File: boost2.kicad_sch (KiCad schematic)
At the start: 37 parts, among them Q1 BSC059N04LS6, Q2 BSC059N04LS6, U1 TPS43061

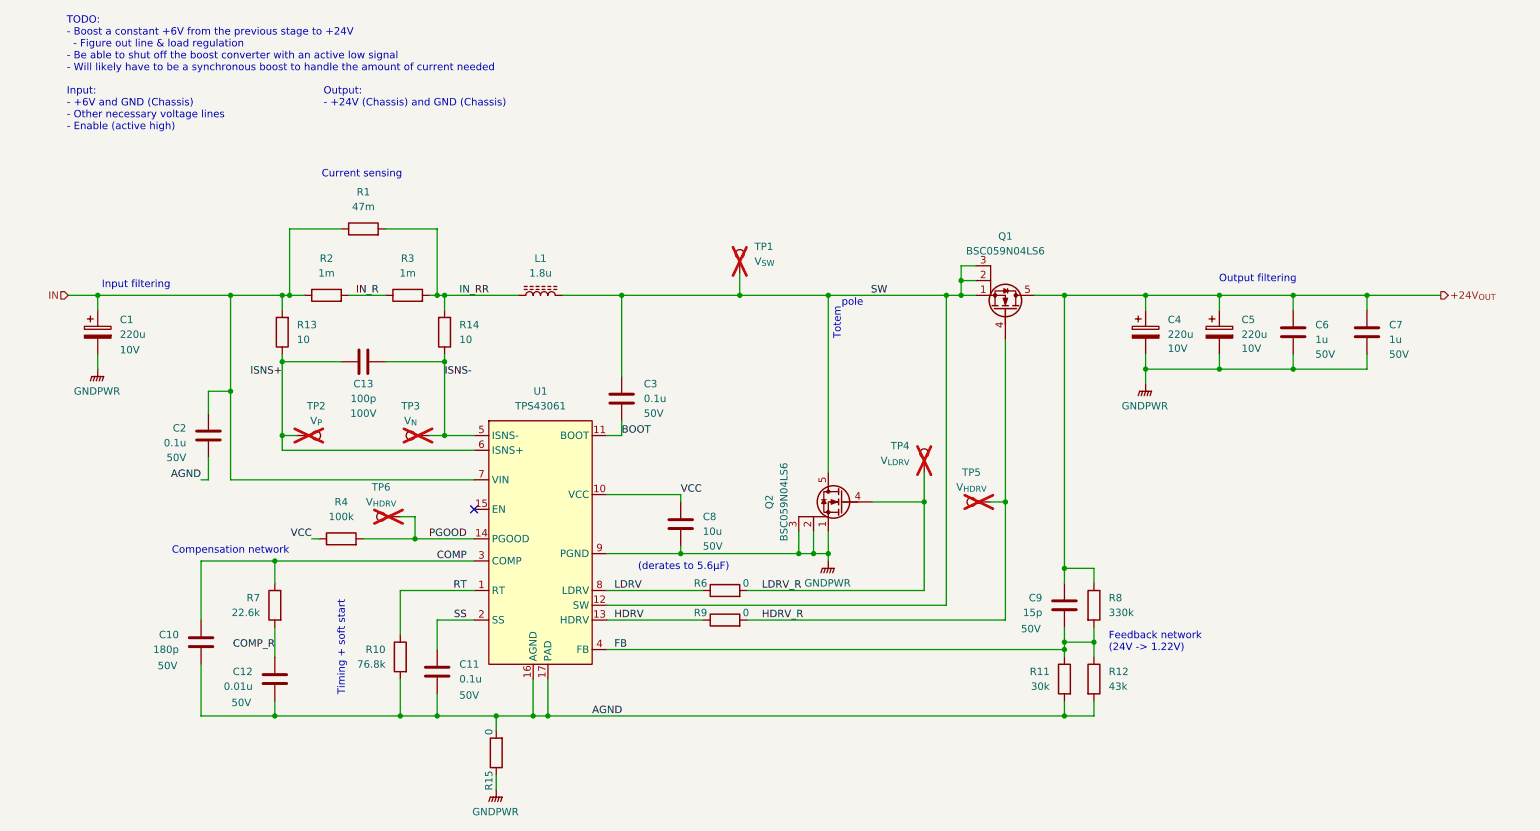
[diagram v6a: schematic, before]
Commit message: Adjust all PCBs and resize boards to be cheaper to order from JLCPCB
Also changed connector pinout to reflect silkscreen
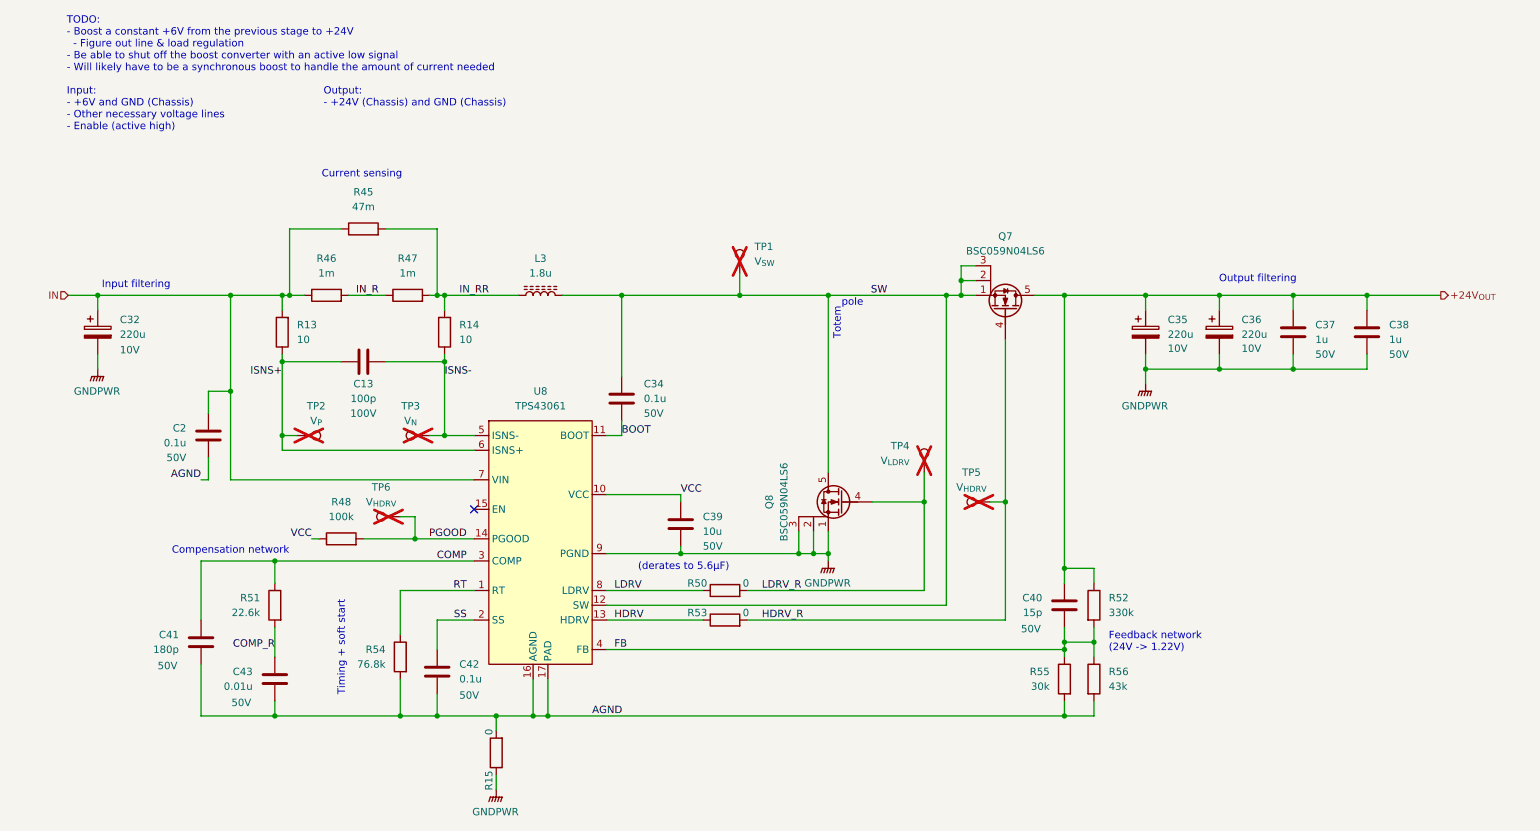
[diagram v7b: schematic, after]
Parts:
- renumbered C1 to C32, C3 to C34, C4 to C35, C5 to C36, C6 to C37, C7 to C38, C8 to C39, C9 to C40, C10 to C41, C11 to C42, C12 to C43, L1 to L3, Q1 to Q7, Q2 to Q8, R1 to R45, R2 to R46, R3 to R47, R4 to R48, R6 to R50, R7 to R51, R8 to R52, R9 to R53, R10 to R54, R11 to R55, R12 to R56, U1 to U8
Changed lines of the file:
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@@
 		(on_board yes)
 		(dnp no)
-		(property "Reference" "C1"
+		(property "Reference" "C32"
 			(at 33.02 72.7709 0)
 			(effects
@@
 		(on_board yes)
 		(dnp no)
-		(property "Reference" "C13"
+		(property "Reference" "C?"
 			(at 74.93 83.82 90)
 			(effects
@@
 				)
 			)
+			(project "SupercapManager"
+				(path "/6197145b-e7d4-44cc-9d90-537b6501bf60/47dffa6f-2678-4be2-969a-7f2e7310ccad"
+					(reference "C?")
+					(unit 1)
+				)
+			)
 		)
 	)
@@
 		(on_board yes)
 		(dnp no)
-		(property "Reference" "C6"
+		(property "Reference" "C37"
 			(at 238.76 73.6599 0)
 			(effects
@@
 		(on_board yes)
 		(dnp no)
-		(property "Reference" "C5"
+		(property "Reference" "C36"
 			(at 226.06 72.7709 0)
 			(effects
@@
 		(dnp no)
 		(fields_autoplaced yes)
-		(property "Reference" "R4"
+		(property "Reference" "R48"
 			(at 71.12 104.14 90)
 			(effects
@@
 		(dnp no)
 		(fields_autoplaced yes)
-		(property "Reference" "R13"
+		(property "Reference" "R?"
 			(at 63.5 73.6599 0)
 			(effects
@@
 				)
 			)
+			(project "SupercapManager"
+				(path "/6197145b-e7d4-44cc-9d90-537b6501bf60/47dffa6f-2678-4be2-969a-7f2e7310ccad"
+					(reference "R?")
+					(unit 1)
+				)
+			)
 		)
 	)
@@
 		(on_board yes)
 		(dnp no)
-		(property "Reference" "R15"
+		(property "Reference" "R?"
 			(at 97.282 150.368 90)
 			(effects
@@
 				)
 			)
+			(project "SupercapManager"
+				(path "/6197145b-e7d4-44cc-9d90-537b6501bf60/47dffa6f-2678-4be2-969a-7f2e7310ccad"
+					(reference "R?")
+					(unit 1)
+				)
+			)
 		)
 	)
@@
 		(dnp no)
 		(fields_autoplaced yes)
-		(property "Reference" "R2"
+		(property "Reference" "R46"
 			(at 68.58 62.23 90)
 			(effects
@@
 		(dnp no)
 		(fields_autoplaced yes)
-		(property "Reference" "#PWR0101"
+		(property "Reference" "#PWR054"
 			(at 29.21 86.36 0)
 			(effects
@@
 		(dnp yes)
 		(fields_autoplaced yes)
-		(property "Reference" "TP1"
+		(property "Reference" "TP?"
 			(at 142.24 60.1979 0)
 			(effects
@@
 		(on_board yes)
 		(dnp no)
-		(property "Reference" "C11"
+		(property "Reference" "C42"
 			(at 91.44 132.0799 0)
 			(effects
@@
 		(on_board yes)
 		(dnp yes)
-		(property "Reference" "TP2"
+		(property "Reference" "TP?"
 			(at 66.802 87.63 90)
 			(effects
@@
 		(on_board yes)
 		(dnp no)
-		(property "Reference" "R11"
+		(property "Reference" "R55"
 			(at 193.04 133.3499 0)
 			(effects
@@
 		(on_board yes)
 		(dnp no)
-		(property "Reference" "Q2"
+		(property "Reference" "Q8"
 			(at 144.78 104.14 90)
 			(effects
@@
 		(on_board yes)
 		(dnp no)
-		(property "Reference" "Q1"
+		(property "Reference" "Q7"
 			(at 185.42 58.42 90)
 			(effects
@@
 		(on_board yes)
 		(dnp no)
-		(property "Reference" "R10"
+		(property "Reference" "R54"
 			(at 78.74 129.5399 0)
 			(effects
@@
 		(on_board yes)
 		(dnp no)
-		(property "Reference" "R7"
+		(property "Reference" "R51"
 			(at 57.15 120.6499 0)
 			(effects
@@
 		(on_board yes)
 		(dnp yes)
-		(property "Reference" "TP4"
+		(property "Reference" "TP?"
 			(at 168.91 94.4879 0)
 			(effects
@@
 		(dnp no)
 		(fields_autoplaced yes)
-		(property "Reference" "#PWR0102"
+		(property "Reference" "#PWR055"
 			(at 209.55 88.9 0)
 			(effects
@@
 		(on_board yes)
 		(dnp no)
-		(property "Reference" "C7"
+		(property "Reference" "C38"
 			(at 251.46 73.6599 0)
 			(effects
@@
 		(on_board yes)
 		(dnp no)
-		(property "Reference" "C12"
+		(property "Reference" "C43"
 			(at 55.88 133.3499 0)
 			(effects
@@
 		(on_board yes)
 		(dnp no)
-		(property "Reference" "C2"
+		(property "Reference" "C?"
 			(at 44.45 91.4399 0)
 			(effects
@@
 				)
 			)
+			(project "SupercapManager"
+				(path "/6197145b-e7d4-44cc-9d90-537b6501bf60/47dffa6f-2678-4be2-969a-7f2e7310ccad"
+					(reference "C?")
+					(unit 1)
+				)
+			)
 		)
 	)
@@
 		(on_board yes)
 		(dnp no)
-		(property "Reference" "R6"
+		(property "Reference" "R50"
 			(at 134.112 118.872 90)
 			(effects
@@
 		(on_board yes)
 		(dnp no)
-		(property "Reference" "C8"
+		(property "Reference" "C39"
 			(at 133.35 106.6799 0)
 			(effects
@@
 		(dnp no)
 		(fields_autoplaced yes)
-		(property "Reference" "R1"
+		(property "Reference" "R45"
 			(at 74.93 50.8 90)
 			(effects
@@
 		(dnp no)
 		(fields_autoplaced yes)
-		(property "Reference" "R14"
+		(property "Reference" "R?"
 			(at 91.44 73.6599 0)
 			(effects
@@
 				)
 			)
+			(project "SupercapManager"
+				(path "/6197145b-e7d4-44cc-9d90-537b6501bf60/47dffa6f-2678-4be2-969a-7f2e7310ccad"
+					(reference "R?")
+					(unit 1)
+				)
+			)
 		)
 	)
@@
 		(dnp yes)
 		(fields_autoplaced yes)
-		(property "Reference" "TP5"
+		(property "Reference" "TP?"
 			(at 179.578 99.06 90)
 			(effects
@@
 		(dnp no)
 		(fields_autoplaced yes)
-		(property "Reference" "U1"
+		(property "Reference" "U8"
 			(at 105.41 85.09 0)
 			(effects
@@
 		(on_board yes)
 		(dnp no)
-		(property "Reference" "C9"
+		(property "Reference" "C40"
 			(at 191.77 120.6499 0)
 			(effects
@@
 		(on_board yes)
 		(dnp no)
-		(property "Reference" "R9"
+		(property "Reference" "R53"
 			(at 134.112 123.952 90)
 			(effects
@@
 		(dnp no)
 		(fields_autoplaced yes)
-		(property "Reference" "#PWR0103"
+		(property "Reference" "#PWR056"
 			(at 154.94 119.38 0)
 			(effects
@@
 		(dnp no)
 		(fields_autoplaced yes)
-		(property "Reference" "R3"
+		(property "Reference" "R47"
 			(at 82.55 62.23 90)
 			(effects
@@
 		(on_board yes)
 		(dnp no)
-		(property "Reference" "C3"
+		(property "Reference" "C34"
 			(at 123.19 83.82 0)
 			(effects
@@
 		(on_board yes)
 		(dnp no)
-		(property "Reference" "C4"
+		(property "Reference" "C35"
 			(at 213.36 72.7709 0)
 			(effects
@@
 		(dnp no)
 		(fields_autoplaced yes)
-		(property "Reference" "R12"
+		(property "Reference" "R56"
 			(at 203.2 133.3499 0)
 			(effects
@@
 		(dnp no)
 		(fields_autoplaced yes)
-		(property "Reference" "L1"
+		(property "Reference" "L3"
 			(at 105.41 62.23 90)
 			(effects
@@
 		(dnp yes)
 		(fields_autoplaced yes)
-		(property "Reference" "TP6"
+		(property "Reference" "TP?"
 			(at 77.978 101.6 90)
 			(effects
@@
 				)
 			)
+			(project "SupercapManager"
+				(path "/6197145b-e7d4-44cc-9d90-537b6501bf60/47dffa6f-2678-4be2-969a-7f2e7310ccad"
+					(reference "TP?")
+					(unit 1)
+				)
+			)
 		)
 	)
@@
 		(on_board yes)
 		(dnp no)
-		(property "Reference" "C10"
+		(property "Reference" "C41"
 			(at 43.18 126.9999 0)
 			(effects
@@
 		(on_board yes)
 		(dnp yes)
-		(property "Reference" "TP3"
+		(property "Reference" "TP?"
 			(at 83.058 87.63 90)
 			(effects
@@
 		(dnp no)
 		(fields_autoplaced yes)
-		(property "Reference" "#PWR0104"
+		(property "Reference" "#PWR?"
 			(at 97.79 158.75 0)
 			(effects
@@
 				)
 			)
+			(project "SupercapManager"
+				(path "/6197145b-e7d4-44cc-9d90-537b6501bf60/47dffa6f-2678-4be2-969a-7f2e7310ccad"
+					(reference "#PWR?")
+					(unit 1)
+				)
+			)
 		)
 	)
@@
 		(dnp no)
 		(fields_autoplaced yes)
-		(property "Reference" "R8"
+		(property "Reference" "R52"
 			(at 203.2 120.6499 0)
 			(effects

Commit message: Replace most banana jacks with XT connectors
+ update library
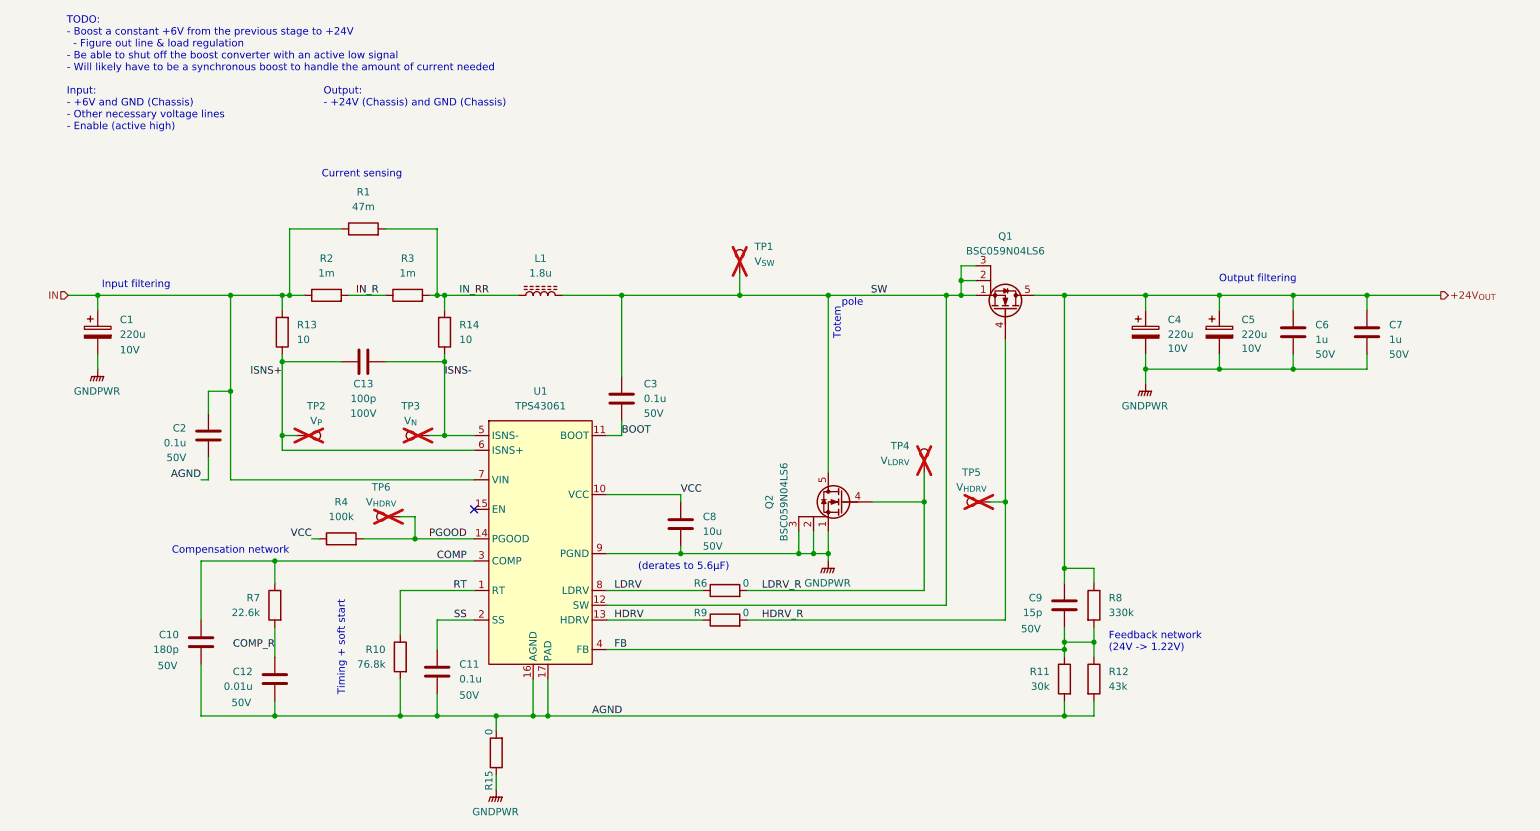
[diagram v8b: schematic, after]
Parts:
- renumbered C32 to C1, C41 to C10, C42 to C11, C43 to C12, C34 to C3, C35 to C4, C36 to C5, C37 to C6, C38 to C7, C39 to C8, C40 to C9, L3 to L1, Q7 to Q1, Q8 to Q2, R45 to R1, R54 to R10, R55 to R11, R56 to R12, R46 to R2, R47 to R3, R48 to R4, R50 to R6, R51 to R7, R52 to R8, R53 to R9, U8 to U1
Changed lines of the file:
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@@
 		(on_board yes)
 		(dnp no)
-		(property "Reference" "C32"
+		(property "Reference" "C1"
 			(at 33.02 72.7709 0)
 			(effects
@@
 		(on_board yes)
 		(dnp no)
-		(property "Reference" "C?"
+		(property "Reference" "C13"
 			(at 74.93 83.82 90)
 			(effects
@@
 		(on_board yes)
 		(dnp no)
-		(property "Reference" "C37"
+		(property "Reference" "C6"
 			(at 238.76 73.6599 0)
 			(effects
@@
 		(on_board yes)
 		(dnp no)
-		(property "Reference" "C36"
+		(property "Reference" "C5"
 			(at 226.06 72.7709 0)
 			(effects
@@
 		(dnp no)
 		(fields_autoplaced yes)
-		(property "Reference" "R48"
+		(property "Reference" "R4"
 			(at 71.12 104.14 90)
 			(effects
@@
 		(dnp no)
 		(fields_autoplaced yes)
-		(property "Reference" "R?"
+		(property "Reference" "R13"
 			(at 63.5 73.6599 0)
 			(effects
@@
 		(on_board yes)
 		(dnp no)
-		(property "Reference" "R?"
+		(property "Reference" "R15"
 			(at 97.282 150.368 90)
 			(effects
@@
 		(dnp no)
 		(fields_autoplaced yes)
-		(property "Reference" "R46"
+		(property "Reference" "R2"
 			(at 68.58 62.23 90)
 			(effects
@@
 		(dnp no)
 		(fields_autoplaced yes)
-		(property "Reference" "#PWR054"
+		(property "Reference" "#PWR0101"
 			(at 29.21 86.36 0)
 			(effects
@@
 		(dnp yes)
 		(fields_autoplaced yes)
-		(property "Reference" "TP?"
+		(property "Reference" "TP1"
 			(at 142.24 60.1979 0)
 			(effects
@@
 		(on_board yes)
 		(dnp no)
-		(property "Reference" "C42"
+		(property "Reference" "C11"
 			(at 91.44 132.0799 0)
 			(effects
@@
 		(on_board yes)
 		(dnp yes)
-		(property "Reference" "TP?"
+		(property "Reference" "TP2"
 			(at 66.802 87.63 90)
 			(effects
@@
 		(on_board yes)
 		(dnp no)
-		(property "Reference" "R55"
+		(property "Reference" "R11"
 			(at 193.04 133.3499 0)
 			(effects
@@
 		(on_board yes)
 		(dnp no)
-		(property "Reference" "Q8"
+		(property "Reference" "Q2"
 			(at 144.78 104.14 90)
 			(effects
@@
 		(on_board yes)
 		(dnp no)
-		(property "Reference" "Q7"
+		(property "Reference" "Q1"
 			(at 185.42 58.42 90)
 			(effects
@@
 		(on_board yes)
 		(dnp no)
-		(property "Reference" "R54"
+		(property "Reference" "R10"
 			(at 78.74 129.5399 0)
 			(effects
@@
 		(on_board yes)
 		(dnp no)
-		(property "Reference" "R51"
+		(property "Reference" "R7"
 			(at 57.15 120.6499 0)
 			(effects
@@
 		(on_board yes)
 		(dnp yes)
-		(property "Reference" "TP?"
+		(property "Reference" "TP4"
 			(at 168.91 94.4879 0)
 			(effects
@@
 		(dnp no)
 		(fields_autoplaced yes)
-		(property "Reference" "#PWR055"
+		(property "Reference" "#PWR0102"
 			(at 209.55 88.9 0)
 			(effects
@@
 		(on_board yes)
 		(dnp no)
-		(property "Reference" "C38"
+		(property "Reference" "C7"
 			(at 251.46 73.6599 0)
 			(effects
@@
 		(on_board yes)
 		(dnp no)
-		(property "Reference" "C43"
+		(property "Reference" "C12"
 			(at 55.88 133.3499 0)
 			(effects
@@
 		(on_board yes)
 		(dnp no)
-		(property "Reference" "C?"
+		(property "Reference" "C2"
 			(at 44.45 91.4399 0)
 			(effects
@@
 		(on_board yes)
 		(dnp no)
-		(property "Reference" "R50"
+		(property "Reference" "R6"
 			(at 134.112 118.872 90)
 			(effects
@@
 		(on_board yes)
 		(dnp no)
-		(property "Reference" "C39"
+		(property "Reference" "C8"
 			(at 133.35 106.6799 0)
 			(effects
@@
 		(dnp no)
 		(fields_autoplaced yes)
-		(property "Reference" "R45"
+		(property "Reference" "R1"
 			(at 74.93 50.8 90)
 			(effects
@@
 		(dnp no)
 		(fields_autoplaced yes)
-		(property "Reference" "R?"
+		(property "Reference" "R14"
 			(at 91.44 73.6599 0)
 			(effects
@@
 		(dnp yes)
 		(fields_autoplaced yes)
-		(property "Reference" "TP?"
+		(property "Reference" "TP5"
 			(at 179.578 99.06 90)
 			(effects
@@
 		(dnp no)
 		(fields_autoplaced yes)
-		(property "Reference" "U8"
+		(property "Reference" "U1"
 			(at 105.41 85.09 0)
 			(effects
@@
 		(on_board yes)
 		(dnp no)
-		(property "Reference" "C40"
+		(property "Reference" "C9"
 			(at 191.77 120.6499 0)
 			(effects
@@
 		(on_board yes)
 		(dnp no)
-		(property "Reference" "R53"
+		(property "Reference" "R9"
 			(at 134.112 123.952 90)
 			(effects
@@
 		(dnp no)
 		(fields_autoplaced yes)
-		(property "Reference" "#PWR056"
+		(property "Reference" "#PWR0103"
 			(at 154.94 119.38 0)
 			(effects
@@
 		(dnp no)
 		(fields_autoplaced yes)
-		(property "Reference" "R47"
+		(property "Reference" "R3"
 			(at 82.55 62.23 90)
 			(effects
@@
 		(on_board yes)
 		(dnp no)
-		(property "Reference" "C34"
+		(property "Reference" "C3"
 			(at 123.19 83.82 0)
 			(effects
@@
 		(on_board yes)
 		(dnp no)
-		(property "Reference" "C35"
+		(property "Reference" "C4"
 			(at 213.36 72.7709 0)
 			(effects
@@
 		(dnp no)
 		(fields_autoplaced yes)
-		(property "Reference" "R56"
+		(property "Reference" "R12"
 			(at 203.2 133.3499 0)
 			(effects
@@
 		(dnp no)
 		(fields_autoplaced yes)
-		(property "Reference" "L3"
+		(property "Reference" "L1"
 			(at 105.41 62.23 90)
 			(effects
@@
 		(dnp yes)
 		(fields_autoplaced yes)
-		(property "Reference" "TP?"
+		(property "Reference" "TP6"
 			(at 77.978 101.6 90)
 			(effects
@@
 		(on_board yes)
 		(dnp no)
-		(property "Reference" "C41"
+		(property "Reference" "C10"
 			(at 43.18 126.9999 0)
 			(effects
@@
 		(on_board yes)
 		(dnp yes)
-		(property "Reference" "TP?"
+		(property "Reference" "TP3"
 			(at 83.058 87.63 90)
 			(effects
@@
 		(dnp no)
 		(fields_autoplaced yes)
-		(property "Reference" "#PWR?"
+		(property "Reference" "#PWR0104"
 			(at 97.79 158.75 0)
 			(effects
@@
 		(dnp no)
 		(fields_autoplaced yes)
-		(property "Reference" "R52"
+		(property "Reference" "R8"
 			(at 203.2 120.6499 0)
 			(effects
